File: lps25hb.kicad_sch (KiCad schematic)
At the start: 4 parts

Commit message: 回路設計済
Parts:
- C11, C12, C13: renamed from C?; footprint (none) -> Capacitor_SMD:C_0603_1608Metric_Pad1.08x0.95mm_HandSolder
- U12: renamed from U?; footprint (none) -> Package_LGA:ST_HLGA-10_2.5x2.5mm_P0.6mm_LayoutBorder3x2y
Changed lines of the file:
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@@
   (symbol (lib_id "My_Device:LPS25HB") (at 153.67 71.12 0) (unit 1)
     (in_bom yes) (on_board yes) (fields_autoplaced)
-    (property "Reference" "U?" (id 0) (at 170.18 79.7812 0))
+    (property "Reference" "U12" (id 0) (at 170.18 79.7812 0))
     (property "Value" "LPS25HB" (id 1) (at 170.18 82.3212 0))
-    (property "Footprint" "" (id 2) (at 153.67 71.12 0)
+    (property "Footprint" "Package_LGA:ST_HLGA-10_2.5x2.5mm_P0.6mm_LayoutBorder3x2y" (id 2) (at 153.67 71.12 0)
       (effects (font (size 1.27 1.27)) hide)
     )
@@
   (symbol (lib_id "power:GND") (at 125.73 78.74 0) (unit 1)
     (in_bom yes) (on_board yes) (fields_autoplaced)
-    (property "Reference" "#PWR?" (id 0) (at 125.73 85.09 0)
+    (property "Reference" "#PWR081" (id 0) (at 125.73 85.09 0)
       (effects (font (size 1.27 1.27)) hide)
     )
@@
   (symbol (lib_id "power:GND") (at 166.37 69.85 0) (unit 1)
     (in_bom yes) (on_board yes) (fields_autoplaced)
-    (property "Reference" "#PWR?" (id 0) (at 166.37 76.2 0)
+    (property "Reference" "#PWR084" (id 0) (at 166.37 76.2 0)
       (effects (font (size 1.27 1.27)) hide)
     )
@@
   (symbol (lib_id "Device:C_Small") (at 134.62 76.2 0) (unit 1)
     (in_bom yes) (on_board yes) (fields_autoplaced)
-    (property "Reference" "C?" (id 0) (at 137.16 74.9362 0)
+    (property "Reference" "C13" (id 0) (at 137.16 74.9362 0)
       (effects (font (size 1.27 1.27)) (justify left))
     )
@@
       (effects (font (size 1.27 1.27)) (justify left))
     )
-    (property "Footprint" "" (id 2) (at 134.62 76.2 0)
+    (property "Footprint" "Capacitor_SMD:C_0603_1608Metric_Pad1.08x0.95mm_HandSolder" (id 2) (at 134.62 76.2 0)
       (effects (font (size 1.27 1.27)) hide)
     )
@@
   (symbol (lib_id "power:GND") (at 144.78 107.95 0) (unit 1)
     (in_bom yes) (on_board yes) (fields_autoplaced)
-    (property "Reference" "#PWR?" (id 0) (at 144.78 114.3 0)
+    (property "Reference" "#PWR083" (id 0) (at 144.78 114.3 0)
       (effects (font (size 1.27 1.27)) hide)
     )
@@
   (symbol (lib_id "Device:C_Small") (at 121.92 91.44 0) (unit 1)
     (in_bom yes) (on_board yes)
-    (property "Reference" "C?" (id 0) (at 116.84 90.17 0)
+    (property "Reference" "C11" (id 0) (at 116.84 90.17 0)
       (effects (font (size 1.27 1.27)) (justify left))
     )
@@
       (effects (font (size 1.27 1.27)) (justify left))
     )
-    (property "Footprint" "" (id 2) (at 121.92 91.44 0)
+    (property "Footprint" "Capacitor_SMD:C_0603_1608Metric_Pad1.08x0.95mm_HandSolder" (id 2) (at 121.92 91.44 0)
       (effects (font (size 1.27 1.27)) hide)
     )
@@
   (symbol (lib_id "power:GND") (at 134.62 78.74 0) (unit 1)
     (in_bom yes) (on_board yes) (fields_autoplaced)
-    (property "Reference" "#PWR?" (id 0) (at 134.62 85.09 0)
+    (property "Reference" "#PWR082" (id 0) (at 134.62 85.09 0)
       (effects (font (size 1.27 1.27)) hide)
     )
@@
   (symbol (lib_id "power:+3.3V") (at 121.92 69.85 0) (unit 1)
     (in_bom yes) (on_board yes) (fields_autoplaced)
-    (property "Reference" "#PWR?" (id 0) (at 121.92 73.66 0)
+    (property "Reference" "#PWR079" (id 0) (at 121.92 73.66 0)
       (effects (font (size 1.27 1.27)) hide)
     )
@@
   (symbol (lib_id "power:GND") (at 121.92 93.98 0) (unit 1)
     (in_bom yes) (on_board yes) (fields_autoplaced)
-    (property "Reference" "#PWR?" (id 0) (at 121.92 100.33 0)
+    (property "Reference" "#PWR080" (id 0) (at 121.92 100.33 0)
       (effects (font (size 1.27 1.27)) hide)
     )
@@
   (symbol (lib_id "Device:C_Small") (at 125.73 76.2 0) (unit 1)
     (in_bom yes) (on_board yes) (fields_autoplaced)
-    (property "Reference" "C?" (id 0) (at 128.27 74.9362 0)
+    (property "Reference" "C12" (id 0) (at 128.27 74.9362 0)
       (effects (font (size 1.27 1.27)) (justify left))
     )
@@
       (effects (font (size 1.27 1.27)) (justify left))
     )
-    (property "Footprint" "" (id 2) (at 125.73 76.2 0)
+    (property "Footprint" "Capacitor_SMD:C_0603_1608Metric_Pad1.08x0.95mm_HandSolder" (id 2) (at 125.73 76.2 0)
       (effects (font (size 1.27 1.27)) hide)
     )

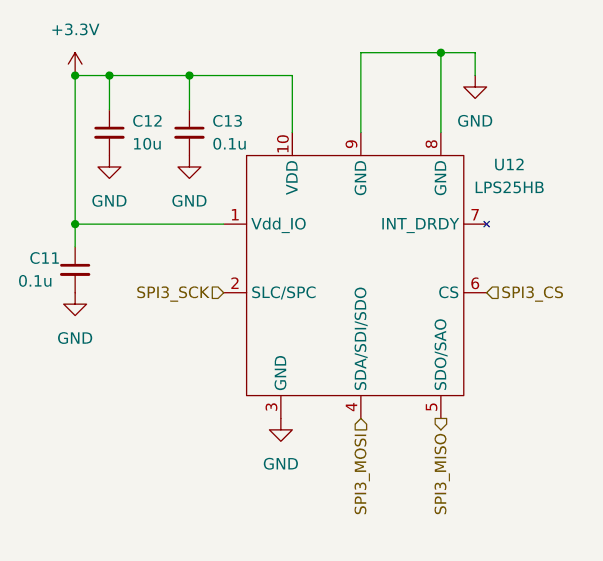
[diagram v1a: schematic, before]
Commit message: 部品配置完了
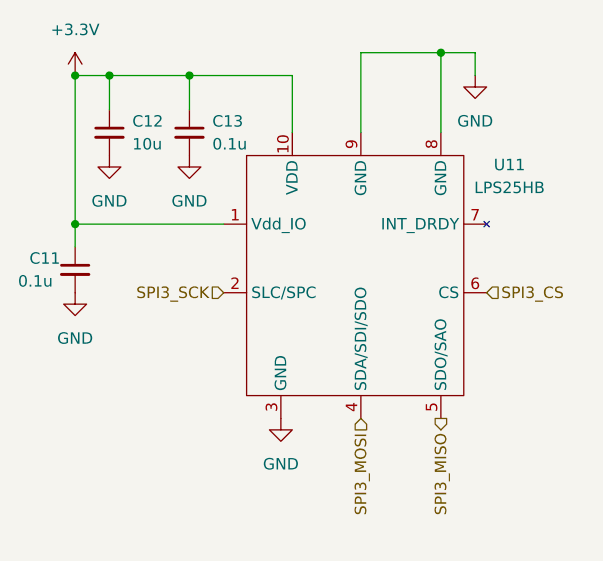
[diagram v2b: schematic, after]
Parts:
- renumbered U12 to U11
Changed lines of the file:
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@@
   (symbol (lib_id "My_Device:LPS25HB") (at 153.67 71.12 0) (unit 1)
     (in_bom yes) (on_board yes) (fields_autoplaced)
-    (property "Reference" "U12" (id 0) (at 170.18 79.7812 0))
+    (property "Reference" "U11" (id 0) (at 170.18 79.7812 0))
     (property "Value" "LPS25HB" (id 1) (at 170.18 82.3212 0))
     (property "Footprint" "Package_LGA:ST_HLGA-10_2.5x2.5mm_P0.6mm_LayoutBorder3x2y" (id 2) (at 153.67 71.12 0)
@@
   (symbol (lib_id "power:GND") (at 125.73 78.74 0) (unit 1)
     (in_bom yes) (on_board yes) (fields_autoplaced)
-    (property "Reference" "#PWR081" (id 0) (at 125.73 85.09 0)
+    (property "Reference" "#PWR029" (id 0) (at 125.73 85.09 0)
       (effects (font (size 1.27 1.27)) hide)
     )
@@
   (symbol (lib_id "power:GND") (at 166.37 69.85 0) (unit 1)
     (in_bom yes) (on_board yes) (fields_autoplaced)
-    (property "Reference" "#PWR084" (id 0) (at 166.37 76.2 0)
+    (property "Reference" "#PWR032" (id 0) (at 166.37 76.2 0)
       (effects (font (size 1.27 1.27)) hide)
     )
@@
   (symbol (lib_id "power:GND") (at 144.78 107.95 0) (unit 1)
     (in_bom yes) (on_board yes) (fields_autoplaced)
-    (property "Reference" "#PWR083" (id 0) (at 144.78 114.3 0)
+    (property "Reference" "#PWR031" (id 0) (at 144.78 114.3 0)
       (effects (font (size 1.27 1.27)) hide)
     )
@@
   (symbol (lib_id "power:GND") (at 134.62 78.74 0) (unit 1)
     (in_bom yes) (on_board yes) (fields_autoplaced)
-    (property "Reference" "#PWR082" (id 0) (at 134.62 85.09 0)
+    (property "Reference" "#PWR030" (id 0) (at 134.62 85.09 0)
       (effects (font (size 1.27 1.27)) hide)
     )
@@
   (symbol (lib_id "power:+3.3V") (at 121.92 69.85 0) (unit 1)
     (in_bom yes) (on_board yes) (fields_autoplaced)
-    (property "Reference" "#PWR079" (id 0) (at 121.92 73.66 0)
+    (property "Reference" "#PWR027" (id 0) (at 121.92 73.66 0)
       (effects (font (size 1.27 1.27)) hide)
     )
@@
   (symbol (lib_id "power:GND") (at 121.92 93.98 0) (unit 1)
     (in_bom yes) (on_board yes) (fields_autoplaced)
-    (property "Reference" "#PWR080" (id 0) (at 121.92 100.33 0)
+    (property "Reference" "#PWR028" (id 0) (at 121.92 100.33 0)
       (effects (font (size 1.27 1.27)) hide)
     )
